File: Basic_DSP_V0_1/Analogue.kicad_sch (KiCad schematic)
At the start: 81 parts, among them J10 53048-0310, J11 53048-0410, J2 53048-0310, J3 53048-0310, J4 53048-0310, J5 53048-0310, J6 53048-0410, J7 53048-0310, J8 53048-0310, J9 53048-0310, U10 TLV9161IDBVR, U6 TLV9161IDBVR, U7 TLV9161IDBVR, U8 TLV9161IDBVR, U9 TLV9161IDBVR

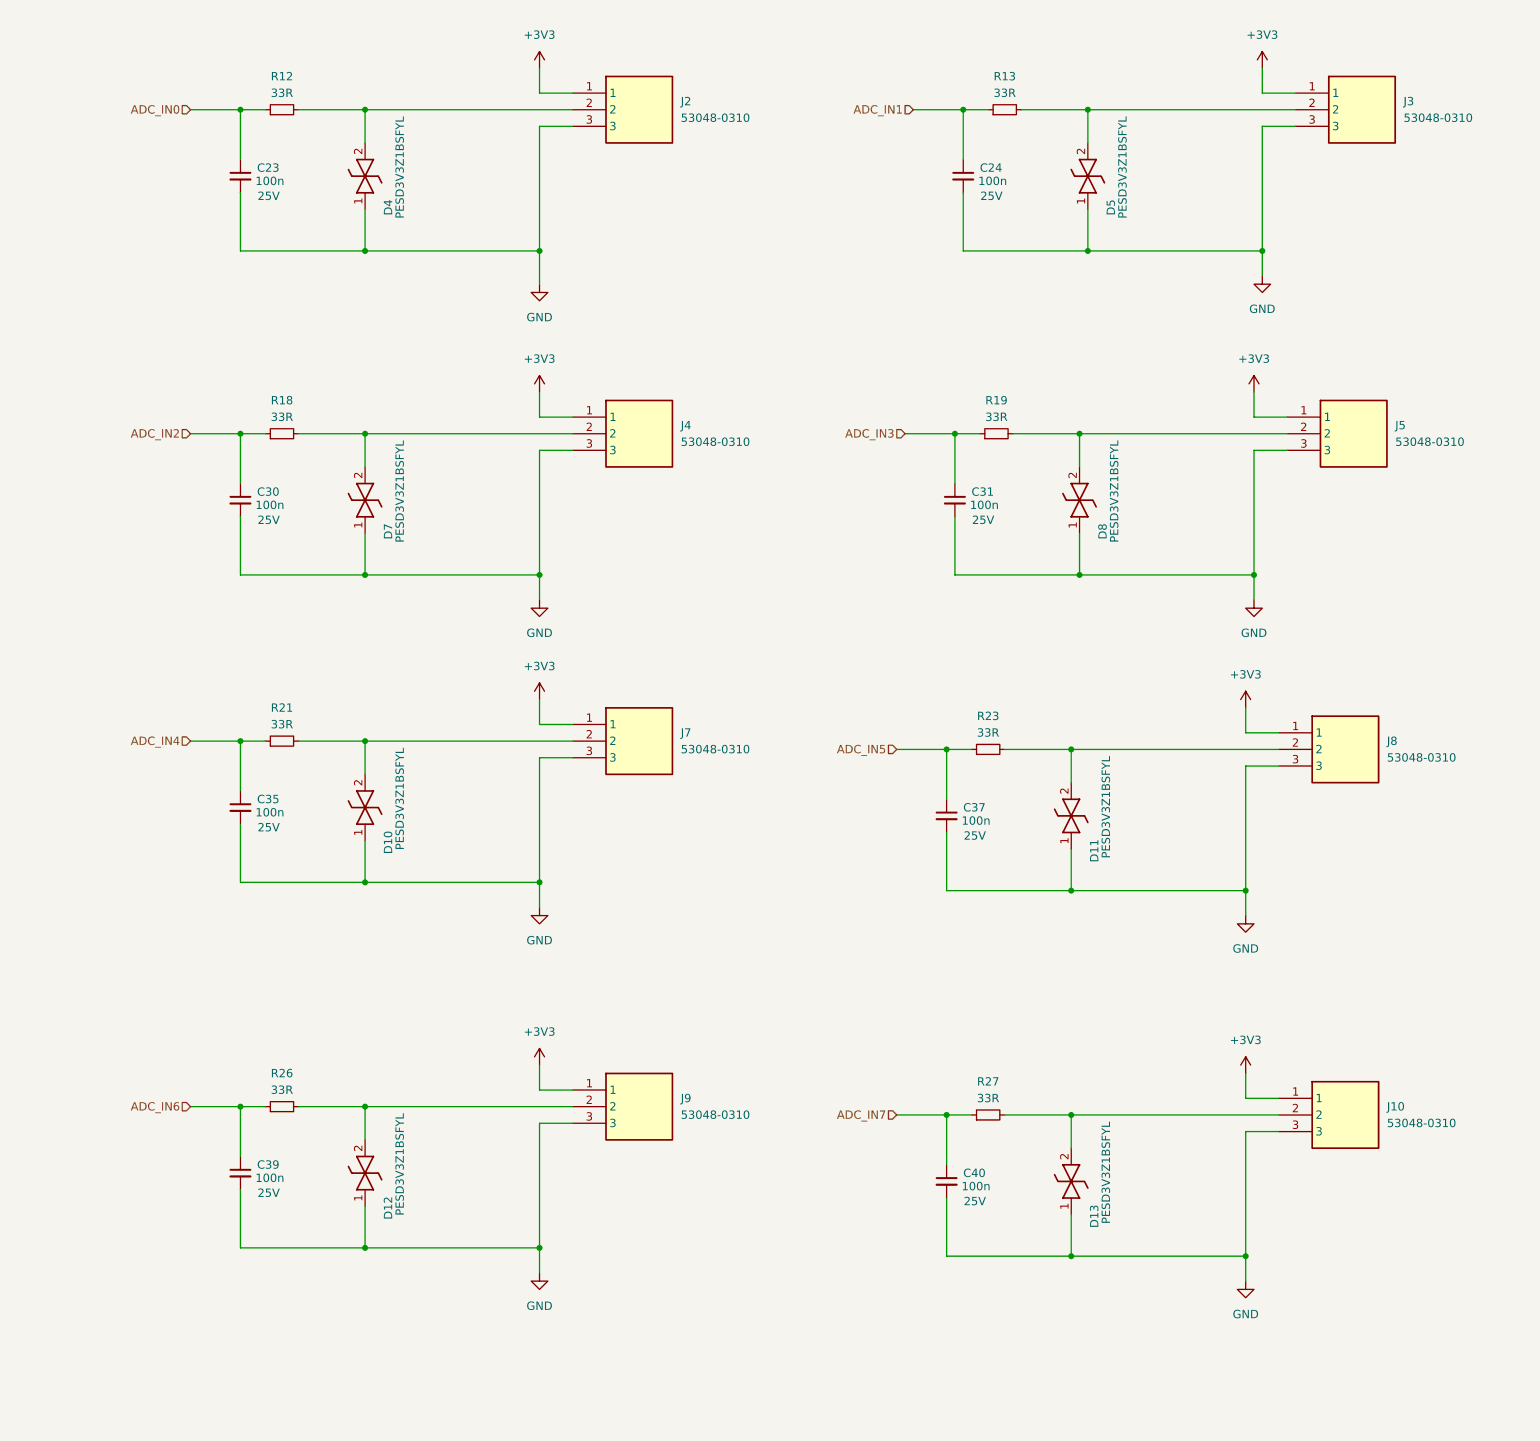
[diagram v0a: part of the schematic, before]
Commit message: Updates to basic DSP schematic
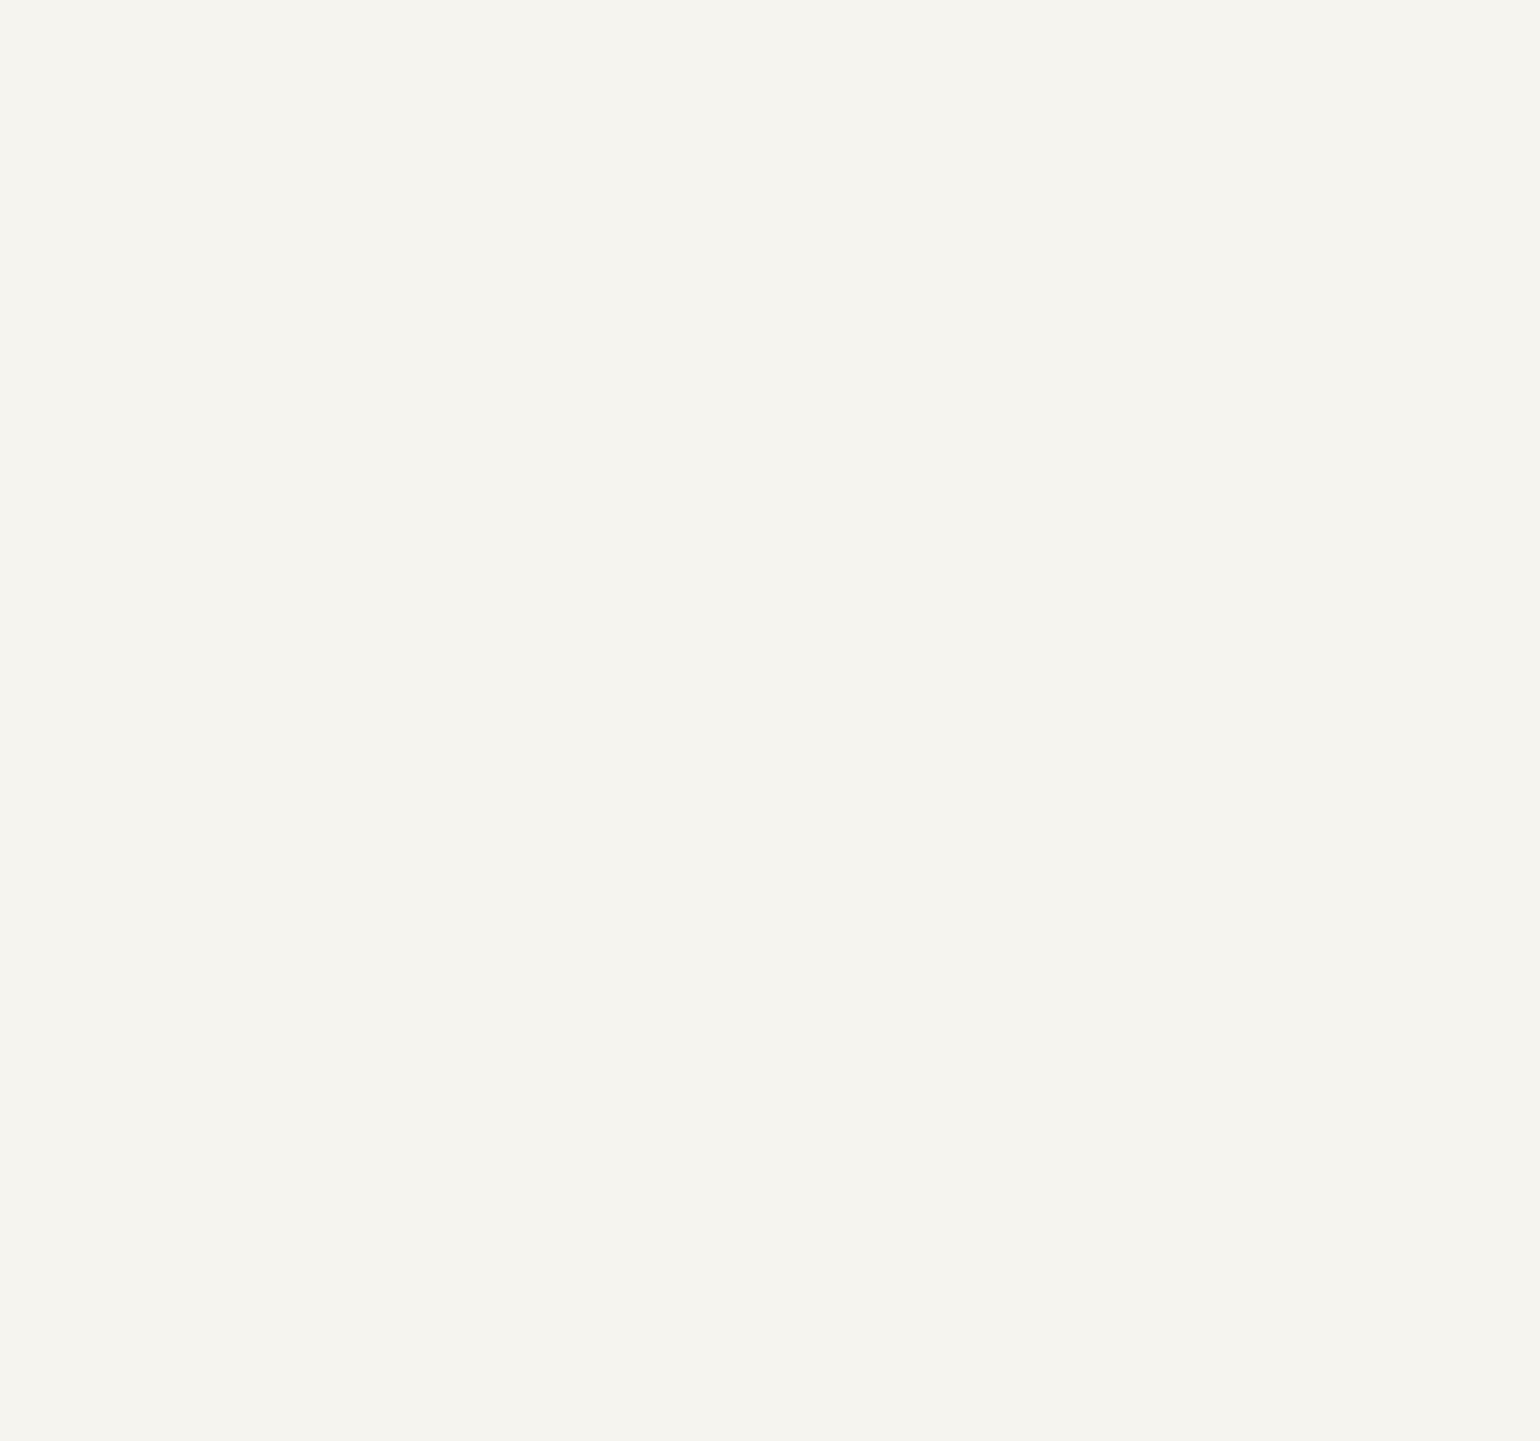
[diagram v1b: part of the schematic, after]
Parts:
- removed C23, C24, C30, C31, C35, C37, C39, C40: 100n, Capacitor_SMD:C_0402_1005Metric, symbol Device:C_Small
- removed D10, D11, D12, D13, D4, D5, D7, D8: PESD3V3Z1BSFYL, symbol Chase_Diode:PESD3V3Z1BSFYL
- removed J10, J2, J3, J4, J5, J7, J8, J9: 53048-0310, Chase_Conn:SHDRRA3W35P0X125_1X3_550X550X350P, symbol Chase_Conn:53048-0310
- removed R12, R13, R18, R19, R21, R23, R26, R27: 33R, Resistor_SMD:R_0402_1005Metric_Pad0.72x0.64mm_HandSolder, symbol Device:R_Small

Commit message: Minor updates to Basic schematic
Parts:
- removed D14, D15, D6, D9: ESD5Z5.0T1G/T5G, Diode_SMD:D_SOD-523, symbol Diode:ESD5Zxx
- added C68, C69, C70, C71, C72: 2u2, Capacitor_SMD:C_0805_2012Metric, symbol Device:C_Small
- added D14, D15, D6, D9: ESD9B5.0ST5G, Diode_SMD:D_SOD-923, symbol Diode:ESD9B5.0ST5G
- C25, C26, C28, C29, C32, C33, C36, C38, C41, C42, C44, C45, C46, C47: footprint Capacitor_SMD:C_0402_1005Metric -> Capacitor_SMD:C_0603_1608Metric_Pad1.08x0.95mm_HandSolder
- C27, C34, C43, C48: footprint Capacitor_SMD:C_0603_1608Metric -> Capacitor_SMD:C_0603_1608Metric_Pad1.08x0.95mm_HandSolder
- R14, R15, R16, R17, R20, R22, R24, R25, R28, R29, R30, R31, R32, R33, R34, R35, R36, R37: footprint Resistor_SMD:R_0402_1005Metric_Pad0.72x0.64mm_HandSolder -> Resistor_SMD:R_0603_1608Metric_Pad0.98x0.95mm_HandSolder
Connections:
- net +5VA: now also C68.1, C69.1, C70.1, C71.1, C72.1
- net AUDIO_IN_L: now also D6.2 (A2)
- net AUDIO_IN_R: now also D9.2 (A2)
- net AUDIO_OUT_L: now also D14.2 (A2)
- net AUDIO_OUT_R: now also D15.2 (A2)
- net GND: now also C68.2, C69.2, C70.2, C71.2, C72.2, D14.1 (A1), D15.1 (A1), D6.1 (A1), D9.1 (A1)

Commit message: Started layout
Removed library from repo as it was messin with the links
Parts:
- C50: footprint Capacitor_SMD:C_0402_1005Metric -> Capacitor_SMD:C_0603_1608Metric_Pad1.08x0.95mm_HandSolder
- J11, J6: footprint (none) -> Chase_Conn:530480410
- U10, U6, U7, U8, U9: footprint (none) -> Chase_OPAMP:SOT95P280X145-5N
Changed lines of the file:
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@@
 			)
 		)
-		(property "Footprint" ""
+		(property "Footprint" "Chase_OPAMP:SOT95P280X145-5N"
 			(at 223.52 177.47 0)
 			(effects
@@
 			)
 		)
-		(property "Footprint" ""
+		(property "Footprint" "Chase_OPAMP:SOT95P280X145-5N"
 			(at 177.8 373.05 0)
 			(effects
@@
 			)
 		)
-		(property "Footprint" "Capacitor_SMD:C_0402_1005Metric"
+		(property "Footprint" "Capacitor_SMD:C_0603_1608Metric_Pad1.08x0.95mm_HandSolder"
 			(at 137.16 350.52 0)
 			(effects
@@
 			)
 		)
-		(property "Footprint" ""
+		(property "Footprint" "Chase_OPAMP:SOT95P280X145-5N"
 			(at 176.53 437.82 0)
 			(effects
@@
 			)
 		)
-		(property "Footprint" ""
+		(property "Footprint" "Chase_OPAMP:SOT95P280X145-5N"
 			(at 222.25 242.24 0)
 			(effects
@@
 			)
 		)
-		(property "Footprint" ""
+		(property "Footprint" "Chase_Conn:530480410"
 			(at 322.58 217.5 0)
 			(effects
@@
 			)
 		)
-		(property "Footprint" ""
+		(property "Footprint" "Chase_Conn:530480410"
 			(at 35.56 18.11 0)
 			(effects
@@
 			)
 		)
-		(property "Footprint" ""
+		(property "Footprint" "Chase_OPAMP:SOT95P280X145-5N"
 			(at 520.7 425.12 0)
 			(effects

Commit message: Updated parts with LCSC order codes
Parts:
- C25, C32, C41, C45, C46: MF TAIYO YUDEN -> FH (Guangdong Fenghua Advanced Tech); MPN MBAST105SB7104KFNA01 -> 0603B104M250NT; OC_LCSC (none) -> C336628
- C26, C33, C42, C47: MF (none) -> TDK; MPN (none) -> CGA3E2X8R2A103KT0Y0H; OC_LCSC (none) -> C445734
- C27, C34, C43, C48: MF Murata Electronics -> Samsung Electro-Mechanics; MPN GRM188R61C106MA73J -> CL10A106MA8NRNC; OC_LCSC (none) -> C96446
- C28, C29, C36, C38: MF (none) -> Walsin Tech Corp; MPN (none) -> 0603N221J500CT; OC_LCSC (none) -> C302062
- C44, C50: MF (none) -> Murata Electronics; MPN (none) -> GCJ188R71H102KA01D; OC_LCSC (none) -> C161114
- C49: footprint Capacitor_SMD:C_1210_3225Metric -> Capacitor_SMD:C_0603_1608Metric_Pad1.08x0.95mm_HandSolder; MF Samsung Electro-Mechanics -> HRE; MPN CL32B226MOJNNNE -> CGA0603X5R226M160JT; OC_LCSC (none) -> C6119868
- C68, C69, C70, C71, C72: footprint Capacitor_SMD:C_0805_2012Metric -> Capacitor_SMD:C_0603_1608Metric_Pad1.08x0.95mm_HandSolder; MF Samsung Electro-Mechanics -> FH (Guangdong Fenghua Advanced Tech); MPN (none) -> 0603B225K250NT; OC_LCSC (none) -> C99228; Voltage (none) -> 25V
- D14, D15, D6, D9: MF (none) -> TECH PUBLIC; MPN (none) -> ESD9B5.0ST5G; OC_LCSC (none) -> C3021104
- J11, J6: MF (none) -> MOLEX; MPN (none) -> 530480410; OC_LCSC (none) -> C588275
- R14, R17, R20, R25, R28, R33: MF (none) -> UNI-ROYAL(Uniroyal Elec); MPN (none) -> 0603WAF1004T5E; OC_LCSC (none) -> C22935
- R15, R22, R30, R35: MF (none) -> YAGEO; MPN (none) -> RC0603FR-07100RL; OC_LCSC (none) -> C105588
- R16, R24, R29, R34: MF (none) -> UNI-ROYAL(Uniroyal Elec); MPN (none) -> 0603WAJ0102T5E; OC_LCSC (none) -> C25585
- R31, R37: MF (none) -> UNI-ROYAL(Uniroyal Elec); MPN (none) -> 0603WAF1002T5E; OC_LCSC (none) -> C25804
- R32, R36: MF (none) -> YAGEO; MPN (none) -> RC0603FR-0747KL; OC_LCSC (none) -> C105579
- U10, U6, U7, U8, U9: MF (none) -> Texas Instruments; MPN (none) -> TLV9161IDBVR; OC_LCSC (none) -> C4368955

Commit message: more layout work on basic DSP
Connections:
- net AUDIO_OUT_L: now also C48.2, D15.2 (A2), J11.3, R37.2; no longer C43.2, D14.2 (A2), J11.1, R31.2
- net AUDIO_OUT_R: now also C43.2, D14.2 (A2), J11.1, R31.2; no longer C48.2, D15.2 (A2), J11.3, R37.2
- net CODEC_OUT_L: now also C47.1; no longer C42.1
- net CODEC_OUT_R: now also C42.1; no longer C47.1
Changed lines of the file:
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@@
-	(wire
-		(pts
-			(xy 64.77 274.32) (xy 96.52 274.32)
-		)
-		(stroke
-			(width 0)
-			(type default)
-		)
-	)
 	(wire
 		(pts
@@
 	(wire
 		(pts
+			(xy 64.77 339.09) (xy 95.25 339.09)
+		)
+		(stroke
+			(width 0)
+			(type default)
+		)
+	)
+	(wire
+		(pts
 			(xy 240.03 57.15) (xy 228.6 57.15)
 		)
@@
 	(wire
 		(pts
-			(xy 63.5 339.09) (xy 95.25 339.09)
-		)
-		(stroke
-			(width 0)
-			(type default)
-		)
-	)
-	(wire
-		(pts
 			(xy 137.16 339.09) (xy 158.75 339.09)
 		)
@@
 		(pts
 			(xy 256.54 156.21) (xy 256.54 167.64)
+		)
+		(stroke
+			(width 0)
+			(type default)
+		)
+	)
+	(wire
+		(pts
+			(xy 96.52 274.32) (xy 63.5 274.32)
 		)
 		(stroke
@@
 	)
 	(label "AUDIO_OUT_R"
-		(at 251.46 342.9 0)
+		(at 260.35 278.13 0)
 		(fields_autoplaced yes)
 		(effects
@@
 	)
 	(label "AUDIO_OUT_L"
-		(at 254 278.13 0)
+		(at 261.62 342.9 0)
 		(fields_autoplaced yes)
 		(effects
@@
 	(hierarchical_label "CODEC_OUT_L"
 		(shape input)
-		(at 64.77 274.32 180)
+		(at 64.77 339.09 180)
 		(fields_autoplaced yes)
 		(effects
@@
 	(hierarchical_label "CODEC_OUT_R"
 		(shape input)
-		(at 63.5 339.09 180)
+		(at 63.5 274.32 180)
 		(fields_autoplaced yes)
 		(effects
